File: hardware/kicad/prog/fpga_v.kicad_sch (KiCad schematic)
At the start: 33 parts, among them J4 PROG V, U13 iCE40HX4K-TQ144, U14 W25Q32JVSS, X2 25 MHz 3,3 V

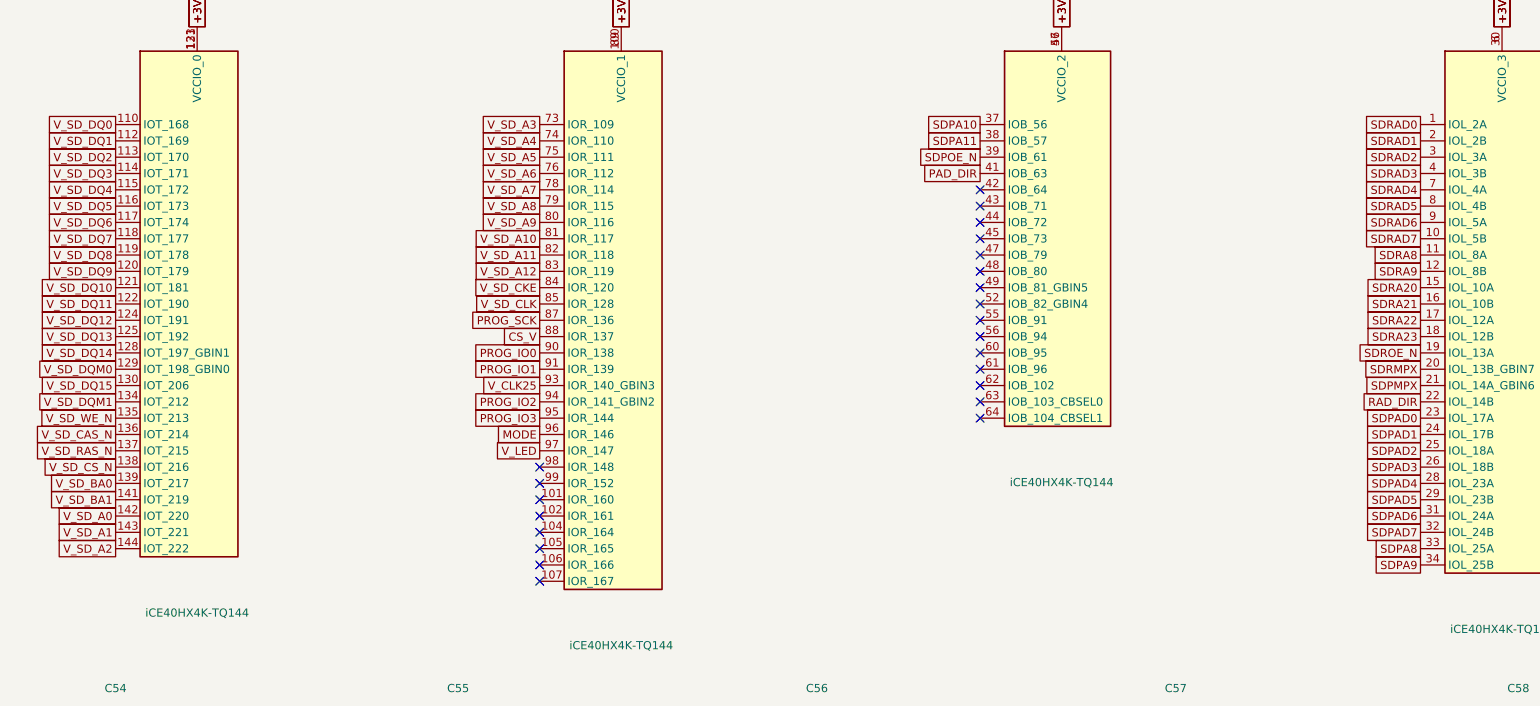
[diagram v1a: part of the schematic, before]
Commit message: Circuits imprimés 2 couches : placement et affectation des broches FPGA
- hardware/gen/pcb.py : empreintes et réseaux depuis boards.py, contour
  depuis outline.py ; ancres placées (contacts, rangée de tampons, FPGA,
  mémoires ; CHA : Pico au centre, microSD et bouton en haut), passifs
  au plus près de leur broche, masse coulée sur les deux faces.
- --pins : signaux des FPGA affectés aux broches tournées vers leur
  cible en conservant l'ordre circulaire (pins_opt.json, repris par
  fpga_pins.py) ; stable en trois passes.
- boards.py : canaux des tampons triés selon la position des contacts.
- hardware/gen/route.py : export Specctra, Freerouting, relecture de la
  session, DRC.
Placement-routage FPGA avec les nouvelles broches : en cours de
vérification.

Co-Authored-By: Claude Opus 5.5 <noreply@anthropic.com>
Claude-Session: https://claude.ai/code/session_01WKfXP1YJ8otGxZ5dsY6Agh
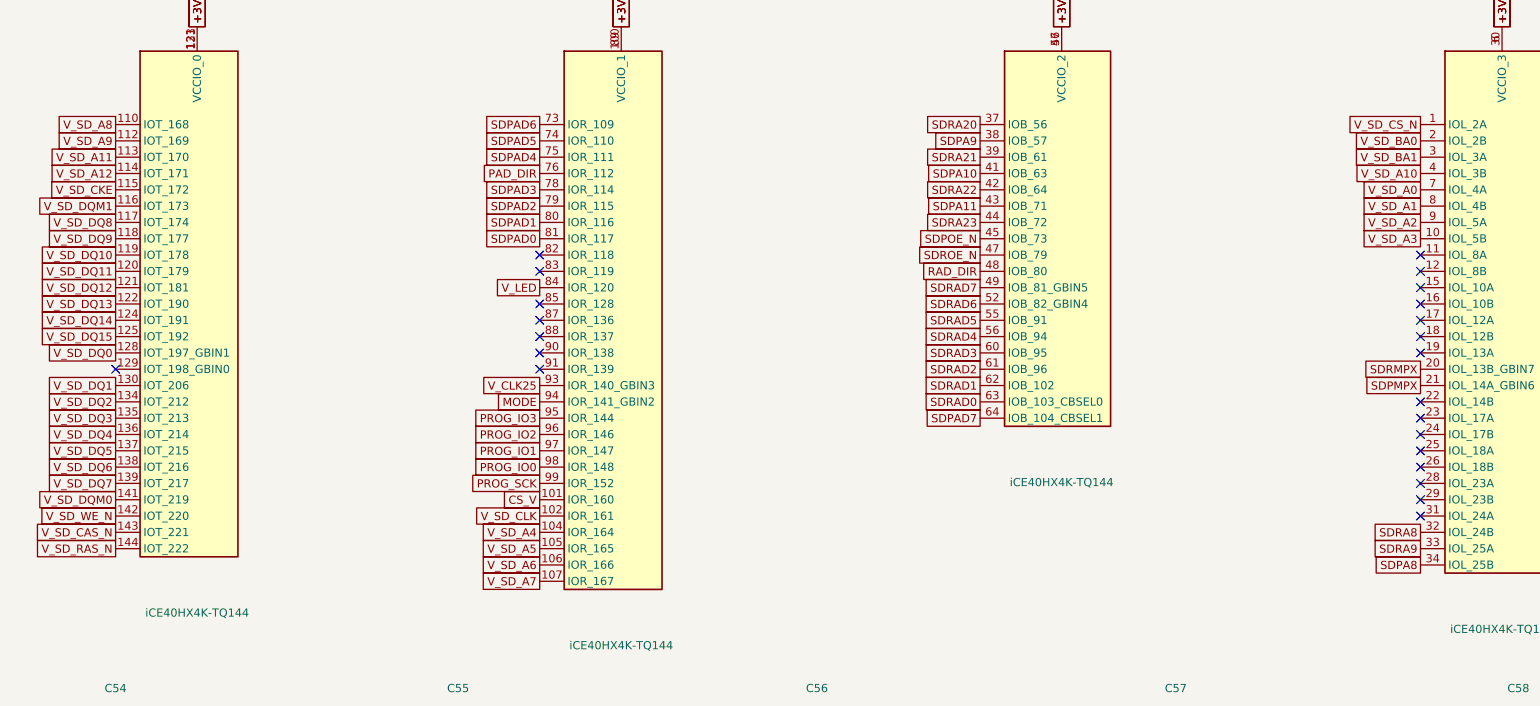
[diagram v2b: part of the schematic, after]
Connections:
- net CS_V: now also U13.101 (IOR_160); no longer U13.88 (IOR_137)
- net MODE: now also U13.94 (IOR_141_GBIN2); no longer U13.96 (IOR_146)
- net PAD_DIR: now also U13.76 (IOR_112); no longer U13.41 (IOB_63)
- net PROG_IO0: now also U13.98 (IOR_148); no longer U13.90 (IOR_138)
- net PROG_IO1: now also U13.97 (IOR_147); no longer U13.91 (IOR_139)
- net PROG_IO2: now also U13.96 (IOR_146); no longer U13.94 (IOR_141_GBIN2)
- net PROG_SCK: now also U13.99 (IOR_152); no longer U13.87 (IOR_136)
- net RAD_DIR: now also U13.48 (IOB_80); no longer U13.22 (IOL_14B)
- net SDPA10: now also U13.41 (IOB_63); no longer U13.37 (IOB_56)
- net SDPA11: now also U13.43 (IOB_71); no longer U13.38 (IOB_57)
- net SDPA8: now also U13.34 (IOL_25B); no longer U13.33 (IOL_25A)
- net SDPA9: now also U13.38 (IOB_57); no longer U13.34 (IOL_25B)
- net SDPAD0: now also U13.81 (IOR_117); no longer U13.23 (IOL_17A)
- net SDPAD1: now also U13.80 (IOR_116); no longer U13.24 (IOL_17B)
- net SDPAD2: now also U13.79 (IOR_115); no longer U13.25 (IOL_18A)
- net SDPAD3: now also U13.78 (IOR_114); no longer U13.26 (IOL_18B)
- net SDPAD4: now also U13.75 (IOR_111); no longer U13.28 (IOL_23A)
- net SDPAD5: now also U13.74 (IOR_110); no longer U13.29 (IOL_23B)
- net SDPAD6: now also U13.73 (IOR_109); no longer U13.31 (IOL_24A)
- net SDPAD7: now also U13.64 (IOB_104_CBSEL1); no longer U13.32 (IOL_24B)
- net SDPOE_N: now also U13.45 (IOB_73); no longer U13.39 (IOB_61)
- net SDRA20: now also U13.37 (IOB_56); no longer U13.15 (IOL_10A)
- net SDRA21: now also U13.39 (IOB_61); no longer U13.16 (IOL_10B)
- net SDRA22: now also U13.42 (IOB_64); no longer U13.17 (IOL_12A)
- net SDRA23: now also U13.44 (IOB_72); no longer U13.18 (IOL_12B)
- net SDRA8: now also U13.32 (IOL_24B); no longer U13.11 (IOL_8A)
- net SDRA9: now also U13.33 (IOL_25A); no longer U13.12 (IOL_8B)
- net SDRAD0: now also U13.63 (IOB_103_CBSEL0); no longer U13.1 (IOL_2A)
- net SDRAD1: now also U13.62 (IOB_102); no longer U13.2 (IOL_2B)
- net SDRAD2: now also U13.61 (IOB_96); no longer U13.3 (IOL_3A)
- net SDRAD3: now also U13.60 (IOB_95); no longer U13.4 (IOL_3B)
- net SDRAD4: now also U13.56 (IOB_94); no longer U13.7 (IOL_4A)
- net SDRAD5: now also U13.55 (IOB_91); no longer U13.8 (IOL_4B)
- net SDRAD6: now also U13.52 (IOB_82_GBIN4); no longer U13.9 (IOL_5A)
- net SDRAD7: now also U13.49 (IOB_81_GBIN5); no longer U13.10 (IOL_5B)
- net SDROE_N: now also U13.47 (IOB_79); no longer U13.19 (IOL_13A)
- net V_LED: now also U13.84 (IOR_120); no longer U13.97 (IOR_147)
- net V_SD_A0: now also U13.7 (IOL_4A); no longer U13.142 (IOT_220)
- net V_SD_A1: now also U13.8 (IOL_4B); no longer U13.143 (IOT_221)
- net V_SD_A10: now also U13.4 (IOL_3B); no longer U13.81 (IOR_117)
- net V_SD_A11: now also U13.113 (IOT_170); no longer U13.82 (IOR_118)
- net V_SD_A12: now also U13.114 (IOT_171); no longer U13.83 (IOR_119)
- net V_SD_A2: now also U13.9 (IOL_5A); no longer U13.144 (IOT_222)
- net V_SD_A3: now also U13.10 (IOL_5B); no longer U13.73 (IOR_109)
- net V_SD_A4: now also U13.104 (IOR_164); no longer U13.74 (IOR_110)
- net V_SD_A5: now also U13.105 (IOR_165); no longer U13.75 (IOR_111)
- net V_SD_A6: now also U13.106 (IOR_166); no longer U13.76 (IOR_112)
- net V_SD_A7: now also U13.107 (IOR_167); no longer U13.78 (IOR_114)
- net V_SD_A8: now also U13.110 (IOT_168); no longer U13.79 (IOR_115)
- net V_SD_A9: now also U13.112 (IOT_169); no longer U13.80 (IOR_116)
- net V_SD_BA0: now also U13.2 (IOL_2B); no longer U13.139 (IOT_217)
- net V_SD_BA1: now also U13.3 (IOL_3A); no longer U13.141 (IOT_219)
- net V_SD_CAS_N: now also U13.143 (IOT_221); no longer U13.136 (IOT_214)
- net V_SD_CKE: now also U13.115 (IOT_172); no longer U13.84 (IOR_120)
- net V_SD_CLK: now also U13.102 (IOR_161); no longer U13.85 (IOR_128)
- net V_SD_CS_N: now also U13.1 (IOL_2A); no longer U13.138 (IOT_216)
- net V_SD_DQ0: now also U13.128 (IOT_197_GBIN1); no longer U13.110 (IOT_168)
- net V_SD_DQ1: now also U13.130 (IOT_206); no longer U13.112 (IOT_169)
- net V_SD_DQ10: now also U13.119 (IOT_178); no longer U13.121 (IOT_181)
- net V_SD_DQ11: now also U13.120 (IOT_179); no longer U13.122 (IOT_190)
- net V_SD_DQ12: now also U13.121 (IOT_181); no longer U13.124 (IOT_191)
- net V_SD_DQ13: now also U13.122 (IOT_190); no longer U13.125 (IOT_192)
- net V_SD_DQ14: now also U13.124 (IOT_191); no longer U13.128 (IOT_197_GBIN1)
- net V_SD_DQ15: now also U13.125 (IOT_192); no longer U13.130 (IOT_206)
- net V_SD_DQ2: now also U13.134 (IOT_212); no longer U13.113 (IOT_170)
- net V_SD_DQ3: now also U13.135 (IOT_213); no longer U13.114 (IOT_171)
- net V_SD_DQ4: now also U13.136 (IOT_214); no longer U13.115 (IOT_172)
- net V_SD_DQ5: now also U13.137 (IOT_215); no longer U13.116 (IOT_173)
- net V_SD_DQ6: now also U13.138 (IOT_216); no longer U13.117 (IOT_174)
- net V_SD_DQ7: now also U13.139 (IOT_217); no longer U13.118 (IOT_177)
- net V_SD_DQ8: now also U13.117 (IOT_174); no longer U13.119 (IOT_178)
- net V_SD_DQ9: now also U13.118 (IOT_177); no longer U13.120 (IOT_179)
- net V_SD_DQM0: now also U13.141 (IOT_219); no longer U13.129 (IOT_198_GBIN0)
- net V_SD_DQM1: now also U13.116 (IOT_173); no longer U13.134 (IOT_212)
- net V_SD_RAS_N: now also U13.144 (IOT_222); no longer U13.137 (IOT_215)
- net V_SD_WE_N: now also U13.142 (IOT_220); no longer U13.135 (IOT_213)

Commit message: FPGA configurés par le RP2350 depuis la carte SD (plus de flash)
- Matériel : flash SPI retirées (4 W25Q32, 12 résistances, 4
  condensateurs). Le bus de liaison arrive sur les broches de
  configuration des iCE40 (LK_SCK -> 70 SCK, LK_IO[0] -> 68 SDI,
  LK_CS_N -> 71 SS), qui redeviennent ces entrées après le démarrage.
  CRESET_N commun aux 4 FPGA, tiré à la masse, piloté par le RP2350
  (GP28) ; câble PROG-CHA en 2 x 7 (CRESET_N + masse). Connecteur 2 x 3
  de secours par FPGA (iceprog -S).
- Firmware : fpga_boot.c (reset commun en mode SPI esclave, envoi des
  SDAES/fpga_*.bin l'un après l'autre, contrôle de CDONE) ; testé sur
  PC (bitstreams reçus à l'identique, FPGA laissés en reset si un
  fichier manque).
- make -C hdl sd : fichiers à copier sur la carte SD.
- PCB : table de placement et références des FPGA mises à jour,
  broches réoptimisées.
Placement-routage des FPGA avec les nouvelles broches : en cours.

Co-Authored-By: Claude Opus 5.5 <noreply@anthropic.com>
Claude-Session: https://claude.ai/code/session_01WKfXP1YJ8otGxZ5dsY6Agh
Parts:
- removed C67, C68: 100n, Capacitor_SMD:C_0603_1608Metric, symbol Device:C
- removed R19: 100, Resistor_SMD:R_0603_1608Metric, symbol Device:R
- removed R20, R21, R22, R23: 10k, Resistor_SMD:R_0603_1608Metric, symbol Device:R
- removed R24: 470, Resistor_SMD:R_0603_1608Metric, symbol Device:R
- removed U13: iCE40HX4K-TQ144, Package_QFP:TQFP-144_20x20mm_P0.5mm, symbol FPGA_Lattice:ICE40HX4K-TQ144
- removed U14: W25Q32JVSS, Package_SO:SOIC-8_5.23x5.23mm_P1.27mm, symbol Memory_Flash:W25Q32JVSS
- added C47: 100n, Capacitor_SMD:C_0603_1608Metric, symbol Device:C
- added R15, R16: 100, Resistor_SMD:R_0603_1608Metric, symbol Device:R
- added R17: 10k, Resistor_SMD:R_0603_1608Metric, symbol Device:R
- added U12: iCE40HX4K-TQ144, Package_QFP:TQFP-144_20x20mm_P0.5mm, symbol FPGA_Lattice:ICE40HX4K-TQ144
- C51, C61, C64: value 100n -> 10u; footprint Capacitor_SMD:C_0603_1608Metric -> Capacitor_SMD:C_0805_2012Metric
- C52, C63, C65: value 10u -> 100n; footprint Capacitor_SMD:C_0805_2012Metric -> Capacitor_SMD:C_0603_1608Metric
- J4: value PROG V -> CONF V
- R18: value 100 -> 470
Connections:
- net V_FL_CS_N is gone; now on net CS_V: J4.2 (Pin_2)
- net V_FL_DO is gone; now on net PROG_IO0: J4.4 (Pin_4)
- net V_FL_SCK is gone; now on net PROG_SCK: J4.1 (Pin_1)
- net +1V2: now also C47.1, R15.1, R16.1, U12.111 (VCC), U12.27 (VCC), U12.40 (VCC), U12.92 (VCC); no longer C52.1, R18.1
- net +3V3: now also C52.1, C66.1, U12.100 (VCCIO_1), U12.108 (VPP_2V5), U12.123 (VCCIO_0), U12.131 (VCCIO_0), U12.30 (VCCIO_3), U12.46 (VCCIO_2), U12.57 (VCCIO_2), U12.6 (VCCIO_3), U12.72 (VCC_SPI), U12.89 (VCCIO_1); no longer C62.1
- net CDONE: now also U12.65 (CDONE)
- net CS_V: now also U12.71 (IOB_108_SS)
- net GND: now also C47.2, R17.2, U12.103 (GND), U12.127 (GNDPLL1), U12.13 (GND), U12.132 (GND), U12.14 (GND), U12.140 (GND), U12.5 (GND), U12.53 (GNDPLL0), U12.59 (GND), U12.69 (GND), U12.86 (GND)
- net MODE: now also U12.96 (IOR_146)
- net PAD_DIR: now also U12.76 (IOR_112)
- net PROG_IO0: now also U12.68 (IOB_106_SDI)
- net PROG_IO1: now also U12.99 (IOR_152)
- net PROG_IO2: now also U12.98 (IOR_148)
- net PROG_IO3: now also U12.97 (IOR_147)
- net PROG_SCK: now also U12.70 (IOB_107_SCK)
- net RAD_DIR: now also U12.48 (IOB_80)
- net SDPA10: now also U12.41 (IOB_63)
- net SDPA11: now also U12.43 (IOB_71)
- net SDPA8: now also U12.34 (IOL_25B)
- net SDPA9: now also U12.38 (IOB_57)
- net SDPAD0: now also U12.81 (IOR_117)
- net SDPAD1: now also U12.80 (IOR_116)
- net SDPAD2: now also U12.79 (IOR_115)
- net SDPAD3: now also U12.78 (IOR_114)
- net SDPAD4: now also U12.75 (IOR_111)
- net SDPAD5: now also U12.74 (IOR_110)
- net SDPAD6: now also U12.73 (IOR_109)
- net SDPAD7: now also U12.64 (IOB_104_CBSEL1)
- net SDPMPX: now also U12.21 (IOL_14A_GBIN6)
- net SDPOE_N: now also U12.45 (IOB_73)
- net SDRA20: now also U12.37 (IOB_56)
- net SDRA21: now also U12.39 (IOB_61)
- net SDRA22: now also U12.42 (IOB_64)
- net SDRA23: now also U12.44 (IOB_72)
- net SDRA8: now also U12.32 (IOL_24B)
- net SDRA9: now also U12.33 (IOL_25A)
- net SDRAD0: now also U12.63 (IOB_103_CBSEL0)
- net SDRAD1: now also U12.62 (IOB_102)
- net SDRAD2: now also U12.61 (IOB_96)
- net SDRAD3: now also U12.60 (IOB_95)
- net SDRAD4: now also U12.56 (IOB_94)
- net SDRAD5: now also U12.55 (IOB_91)
- net SDRAD6: now also U12.52 (IOB_82_GBIN4)
- net SDRAD7: now also U12.49 (IOB_81_GBIN5)
- net SDRMPX: now also U12.20 (IOL_13B_GBIN7)
- net SDROE_N: now also U12.47 (IOB_79)
- net V_CLK25: now also U12.93 (IOR_140_GBIN3)
- net V_LED: now also R18.1, U12.88 (IOR_137)
- net V_LED_K: now also R18.2
- net V_SD_A0: now also U12.4 (IOL_3B)
- net V_SD_A1: now also U12.7 (IOL_4A)
- net V_SD_A10: now also U12.3 (IOL_3A)
- net V_SD_A11: now also U12.112 (IOT_169)
- net V_SD_A12: now also U12.113 (IOT_170)
- net V_SD_A2: now also U12.8 (IOL_4B)
- net V_SD_A3: now also U12.9 (IOL_5A)
- net V_SD_A4: now also U12.102 (IOR_161)
- net V_SD_A5: now also U12.104 (IOR_164)
- net V_SD_A6: now also U12.105 (IOR_165)
- net V_SD_A7: now also U12.106 (IOR_166)
- net V_SD_A8: now also U12.107 (IOR_167)
- net V_SD_A9: now also U12.110 (IOT_168)
- net V_SD_BA0: now also U12.1 (IOL_2A)
- net V_SD_BA1: now also U12.2 (IOL_2B)
- net V_SD_CAS_N: now also U12.142 (IOT_220)
- net V_SD_CKE: now also U12.114 (IOT_171)
- net V_SD_CLK: now also U12.101 (IOR_160)
- net V_SD_CS_N: now also U12.144 (IOT_222)
- net V_SD_DQ0: now also U12.125 (IOT_192)
- net V_SD_DQ1: now also U12.128 (IOT_197_GBIN1)
- net V_SD_DQ10: now also U12.118 (IOT_177)
- net V_SD_DQ11: now also U12.119 (IOT_178)
- net V_SD_DQ12: now also U12.120 (IOT_179)
- net V_SD_DQ13: now also U12.121 (IOT_181)
- net V_SD_DQ14: now also U12.122 (IOT_190)
- net V_SD_DQ15: now also U12.124 (IOT_191)
- net V_SD_DQ2: now also U12.130 (IOT_206)
- net V_SD_DQ3: now also U12.134 (IOT_212)
- net V_SD_DQ4: now also U12.135 (IOT_213)
- net V_SD_DQ5: now also U12.136 (IOT_214)
- net V_SD_DQ6: now also U12.137 (IOT_215)
- net V_SD_DQ7: now also U12.138 (IOT_216)
- net V_SD_DQ8: now also U12.116 (IOT_173)
- net V_SD_DQ9: now also U12.117 (IOT_174)
- net V_SD_DQM0: now also U12.139 (IOT_217)
- net V_SD_DQM1: now also U12.115 (IOT_172)
- net V_SD_RAS_N: now also U12.143 (IOT_221)
- net V_SD_WE_N: now also U12.141 (IOT_219)
- net V_VCCPLL0: now also C62.1, R15.2, U12.54 (VCCPLL0); no longer C64.1, R18.2
- net V_VCCPLL1: now also C64.1, R16.2, U12.126 (VCCPLL1); no longer C66.1
- net V_CRESET_N renamed CRESET_N
- net CRESET_N: now also R17.1, U12.66 (~{CRESET})
- net V_FL_DI renamed V_SDO
- net V_SDO: now also U12.67 (IOB_105_SDO)
- no-connect marks 31 -> 34

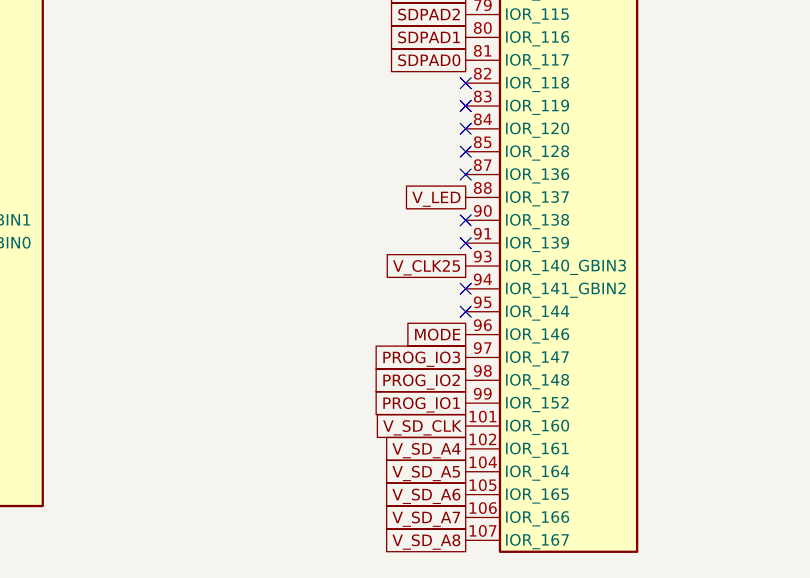
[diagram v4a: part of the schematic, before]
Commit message: Pico 2, microSD et bouton sur la carte PROG ; pistes d'alimentation larges
- La carte PROG est côté avant de la cartouche, composants vers l'avant :
  lecteur microSD et bouton accessibles. Le câble PROG-CHA porte
  désormais le bus de liaison C/SM ; connecteur au même endroit sur les
  deux cartes (x = 172 mm), prêt pour un connecteur carte à carte.
- Sous le Pico : ni piste ni via sur la face composants (pastilles de
  test nues sous le module).
- Classes de réseaux écrites dans le .kicad_pro : +5V et VSYS en 0,5 mm,
  +1V2 en 0,3 mm.
- Broches des FPGA réoptimisées ; contrôle Freerouting sans violation ;
  routage des deux cartes et vérification de timing en cours.

Co-Authored-By: Claude Opus 5.5 <noreply@anthropic.com>
Claude-Session: https://claude.ai/code/session_01WKfXP1YJ8otGxZ5dsY6Agh
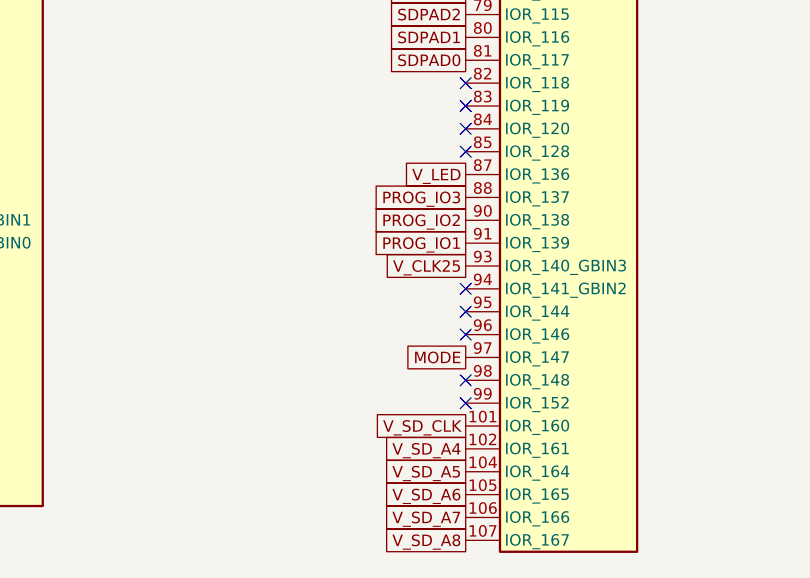
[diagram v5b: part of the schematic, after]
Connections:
- net MODE: now also U12.97 (IOR_147); no longer U12.96 (IOR_146)
- net PROG_IO1: now also U12.91 (IOR_139); no longer U12.99 (IOR_152)
- net PROG_IO2: now also U12.90 (IOR_138); no longer U12.98 (IOR_148)
- net PROG_IO3: now also U12.88 (IOR_137); no longer U12.97 (IOR_147)
- net V_LED: now also U12.87 (IOR_136); no longer U12.88 (IOR_137)
